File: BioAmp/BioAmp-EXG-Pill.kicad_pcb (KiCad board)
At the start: 4 copper layers, 48.2 x 13.2 mm, 43 parts, among them IC3 MAX1169BEUD+, J1 Conn_01x06_Pin, J2 Conn_01x06_Pin, J4 522710469, U1 TL074HIPWR

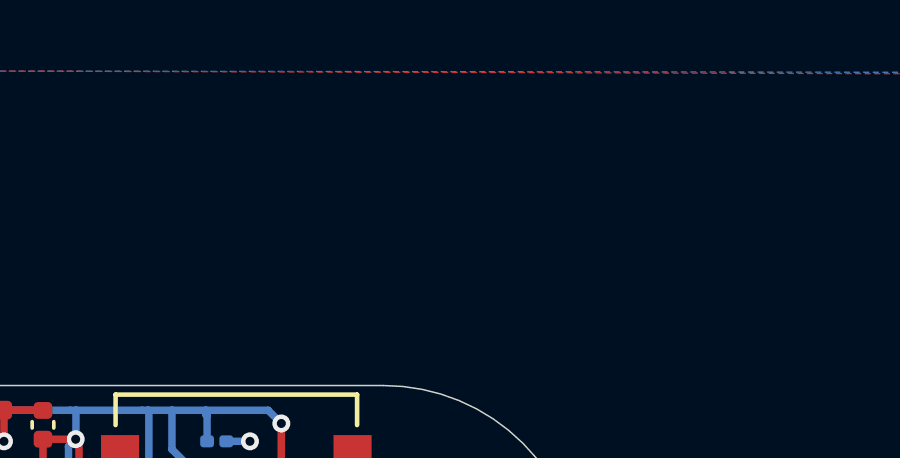
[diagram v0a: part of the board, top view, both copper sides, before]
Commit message: Changed schematics to new ADC ADS
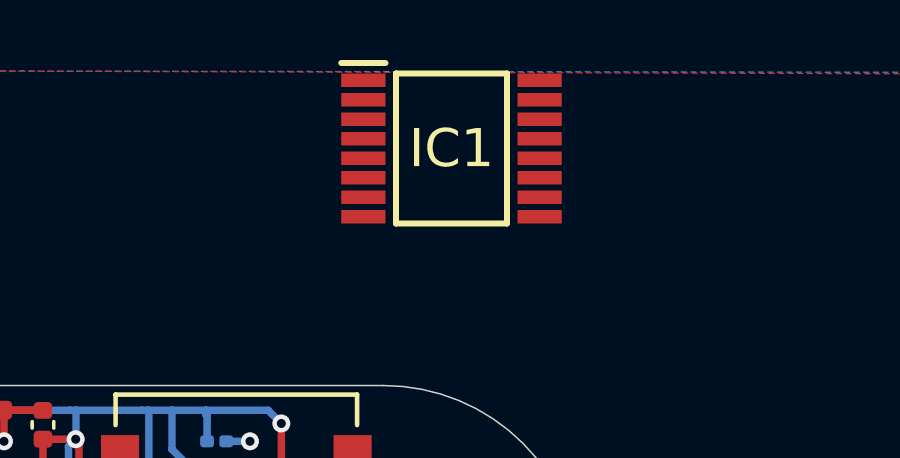
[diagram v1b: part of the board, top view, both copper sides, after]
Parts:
- added IC1: ADS112C04IPW, New_ADS112C04:SOP65P640X120-16N, F.Cu at (147.9, 79.1)

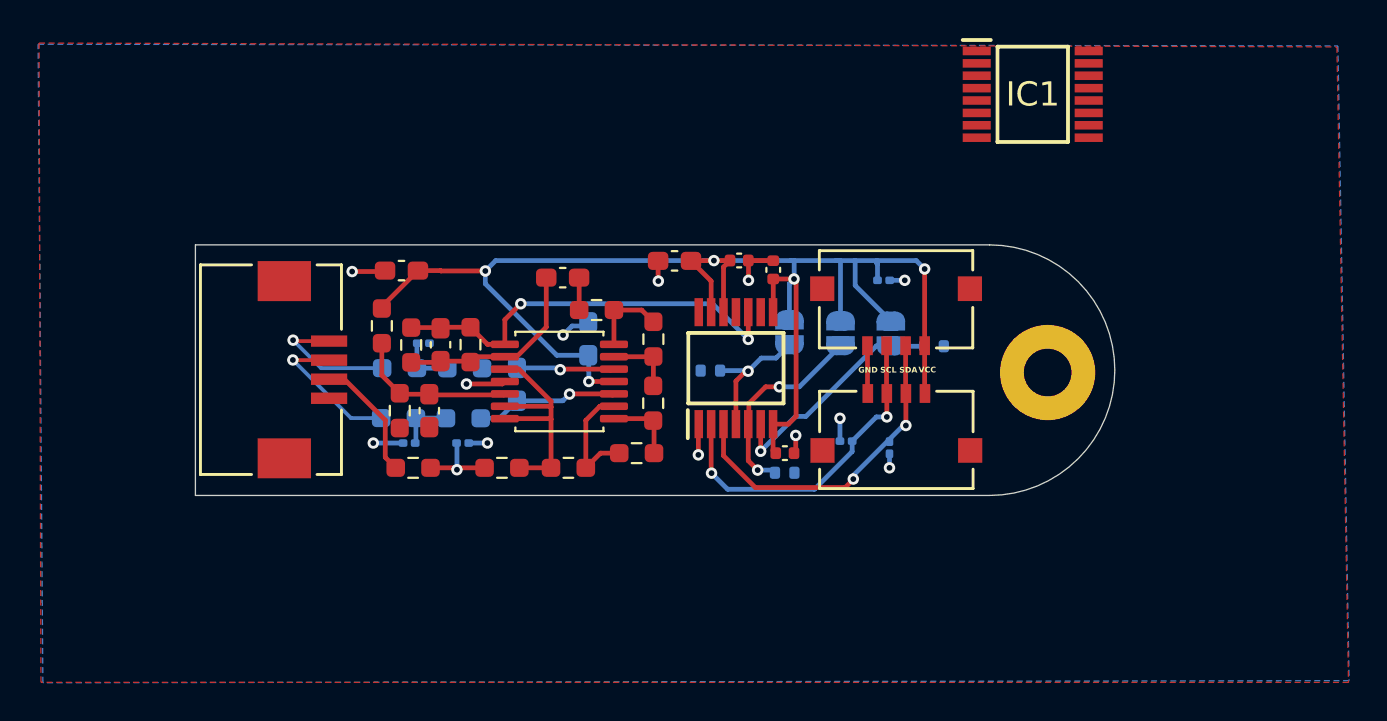
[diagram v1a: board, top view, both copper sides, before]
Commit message: Finished layout with new ADC - ADS
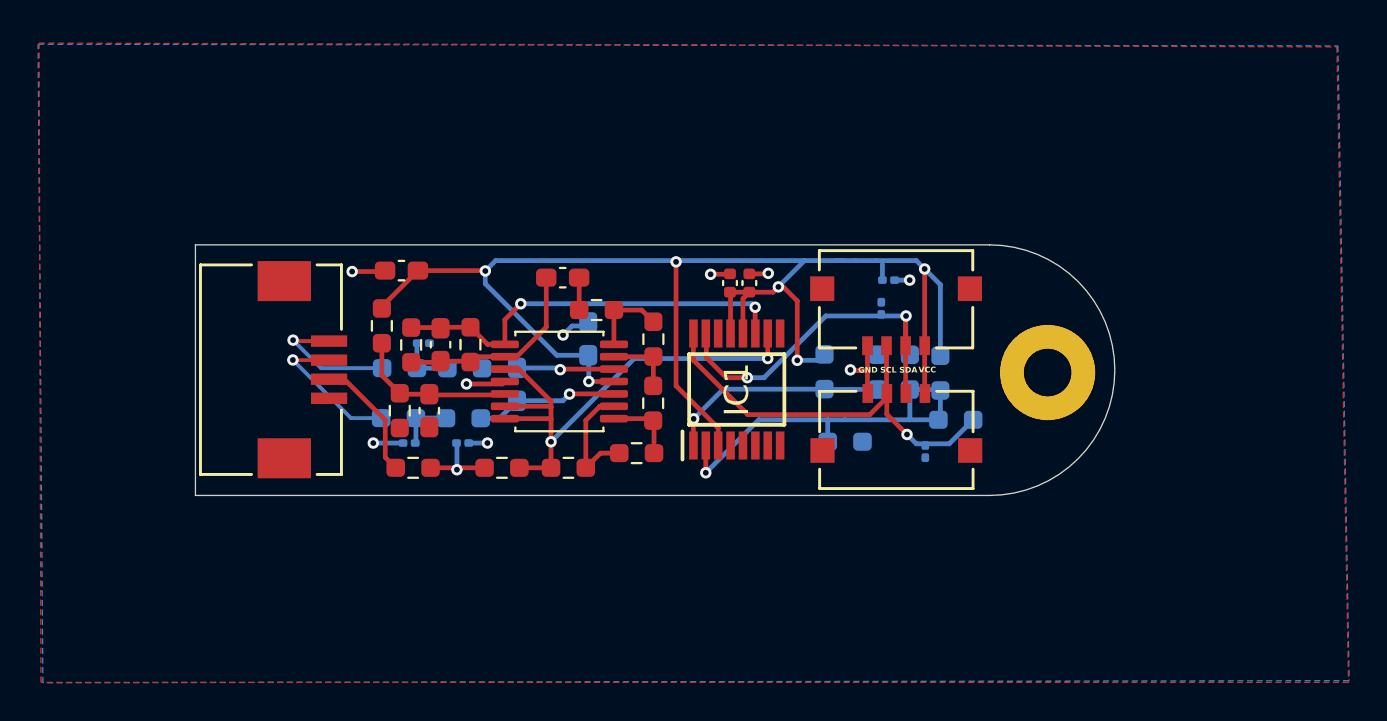
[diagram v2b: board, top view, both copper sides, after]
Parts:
- removed C10: 100n, Capacitor_SMD:C_0402_1005Metric
- removed C12: 10u, Capacitor_SMD:C_0603_1608Metric_Pad1.08x0.95mm_HandSolder
- removed IC3: MAX1169BEUD+, MAX1169:SOP65P640X110-14N
- removed JP4, JP5, JP6: SolderJumper_2_Open, Jumper:SolderJumper-2_P1.3mm_Open_RoundedPad1.0x1.5mm
- added R16: 10k, Resistor_SMD:R_0603_1608Metric_Pad0.98x0.95mm_HandSolder, B.Cu at (137.0, 93.7)
- added R20: 10k, Resistor_SMD:R_0603_1608Metric_Pad0.98x0.95mm_HandSolder, B.Cu at (143.9, 96.2)
- added R21: 10k, Resistor_SMD:R_0603_1608Metric_Pad0.98x0.95mm_HandSolder, B.Cu at (141.5, 93.7)
- R17, R18, R19: footprint Resistor_SMD:R_0402_1005Metric -> Resistor_SMD:R_0603_1608Metric_Pad0.98x0.95mm_HandSolder
- moved IC1 21.9 mm to (132.4, 94.6), turned to 90 degrees
- moved R18 9.70 mm to (143.1, 93.7), turned to -90 degrees
- moved R17 8.77 mm to (139.8, 93.7), turned to 90 degrees
- moved D5 7.33 mm to (140.0, 90.3), turned to 90 degrees
- moved R19 6.85 mm to (138.1, 97.3)
- moved D6 4.20 mm to (142.3, 97.8), turned to -90 degrees
- moved C9 2.37 mm to (132.0, 89.0)
- moved C11 1.30 mm to (133.0, 89.0), turned to -90 degrees
- moved D4 0.26 mm to (140.3, 88.8)
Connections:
- IC1 pad 1: unconnected-(IC1-A0-Pad1) -> /ADD0
- IC1 pad 10: unconnected-(IC1-AIN1-Pad10) -> ampRef
- IC1 pad 11: unconnected-(IC1-AIN0-Pad11) -> bpfOUT
- IC1 pad 12: unconnected-(IC1-AVDD-Pad12) -> VCC
- IC1 pad 13: unconnected-(IC1-DVDD-Pad13) -> VCC
- IC1 pad 15: unconnected-(IC1-SDA-Pad15) -> SDA
- IC1 pad 16: unconnected-(IC1-SCL-Pad16) -> SCL
- IC1 pad 2: unconnected-(IC1-A1-Pad2) -> /ADD1
- IC1 pad 3: unconnected-(IC1-~{RESET}-Pad3) -> VCC
- IC1 pad 4: unconnected-(IC1-DGND-Pad4) -> GND
- IC1 pad 5: unconnected-(IC1-AVSS-Pad5) -> GND
- R17 pad 1: /ADD2 -> /ADD0
- R18 pad 1: /ADD1 -> VCC
- R18 pad 2: GND -> /ADD1
- R19 pad 1: /ADD0 -> /ADD1
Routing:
- net ampRef: track 13.2 -> 27.6 mm, vias 0 -> 2
- net /ADD1: track 10.7 -> 20.9 mm, vias 2 -> 1
- net /ADD2: track 7.53 -> 0.00 mm, vias 1 -> 0
- net GND: track 19.3 -> 14.2 mm, vias 12 -> 9
- net SCL: track 17.8 -> 22.6 mm, vias 2 -> 1
- net SDA: track 17.7 -> 19.8 mm
- net VCC: track 79.1 -> 77.9 mm, vias 5 -> 6
- net /ADD0: track 12.6 -> 11.7 mm

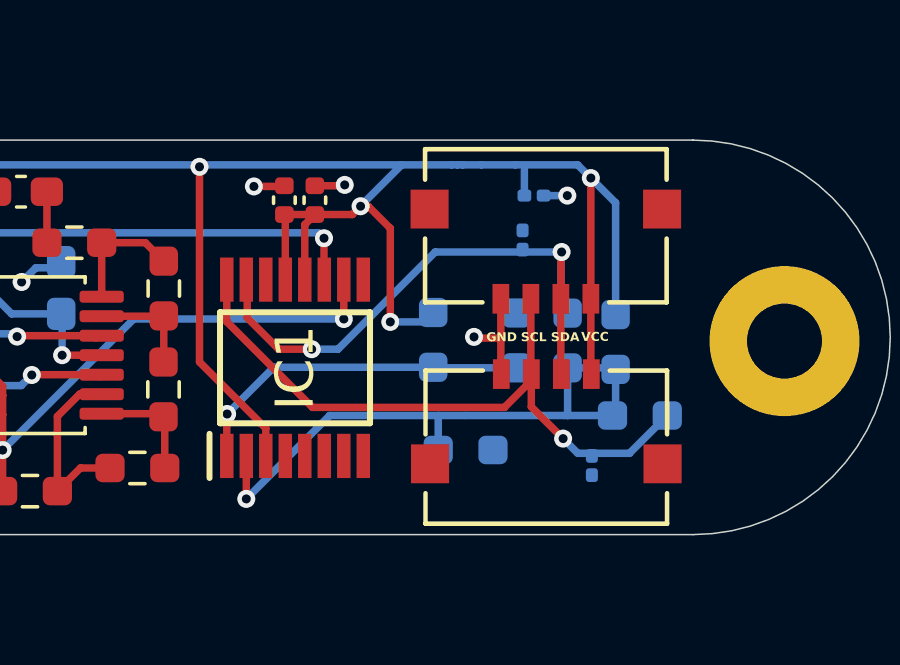
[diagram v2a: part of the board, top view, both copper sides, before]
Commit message: Changed position of TVS on SCL
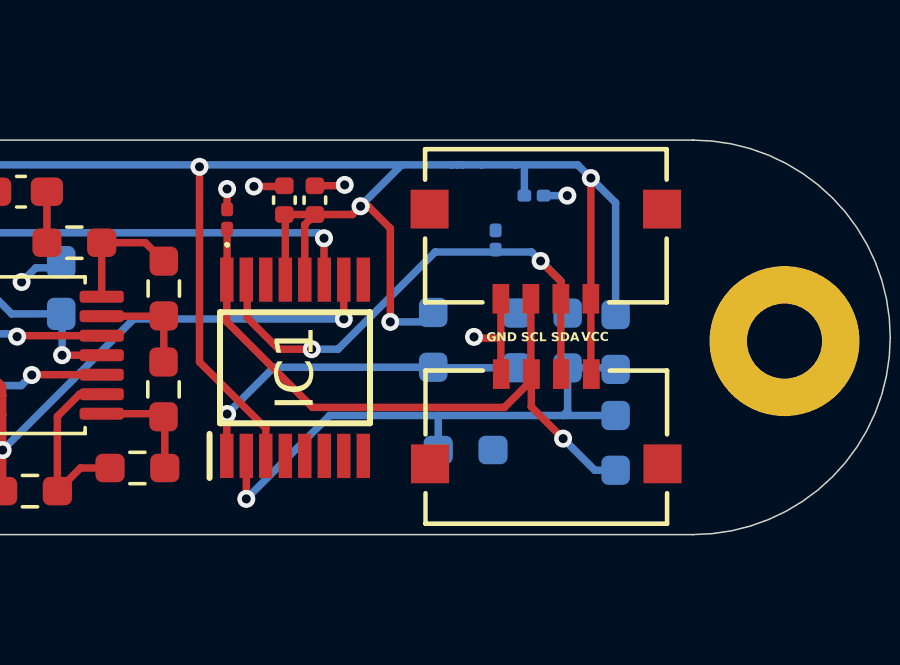
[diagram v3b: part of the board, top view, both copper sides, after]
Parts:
- D6: moved to F.Cu
- moved D6 14.7 mm to (130.1, 89.6), turned to 90 degrees
- moved R20 1.22 mm to (143.1, 97.1), turned to -90 degrees
- moved D5 0.90 mm to (139.1, 90.3)
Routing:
- net /ADD1: track 20.9 -> 19.4 mm
- net GND: track 14.2 -> 14.9 mm, vias 9 -> 10
- net SDA: track 19.8 -> 19.1 mm

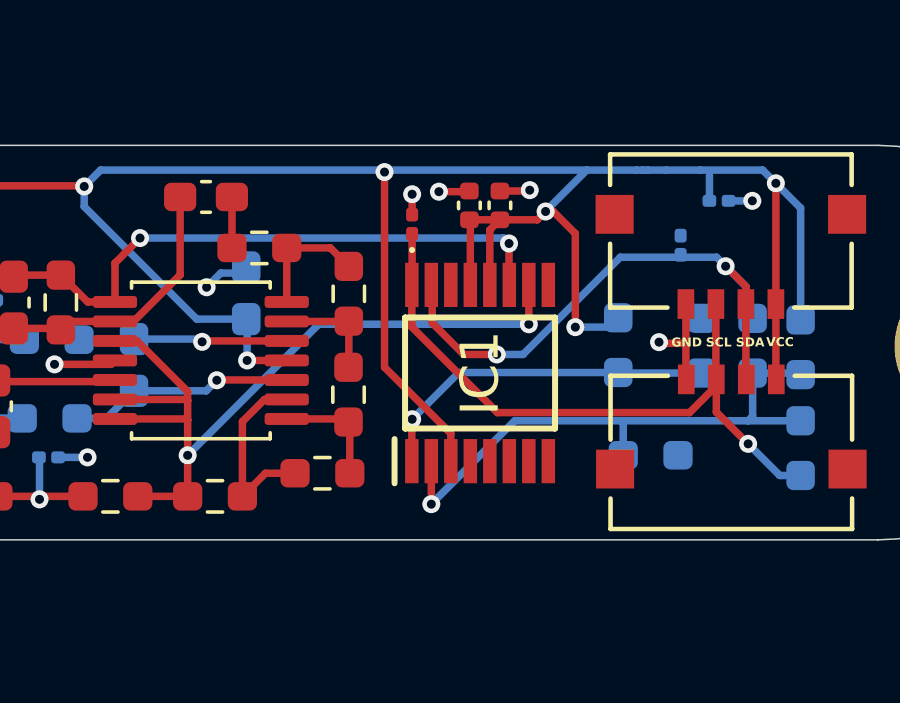
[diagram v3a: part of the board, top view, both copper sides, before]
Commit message: Added via to GND pins on ADC
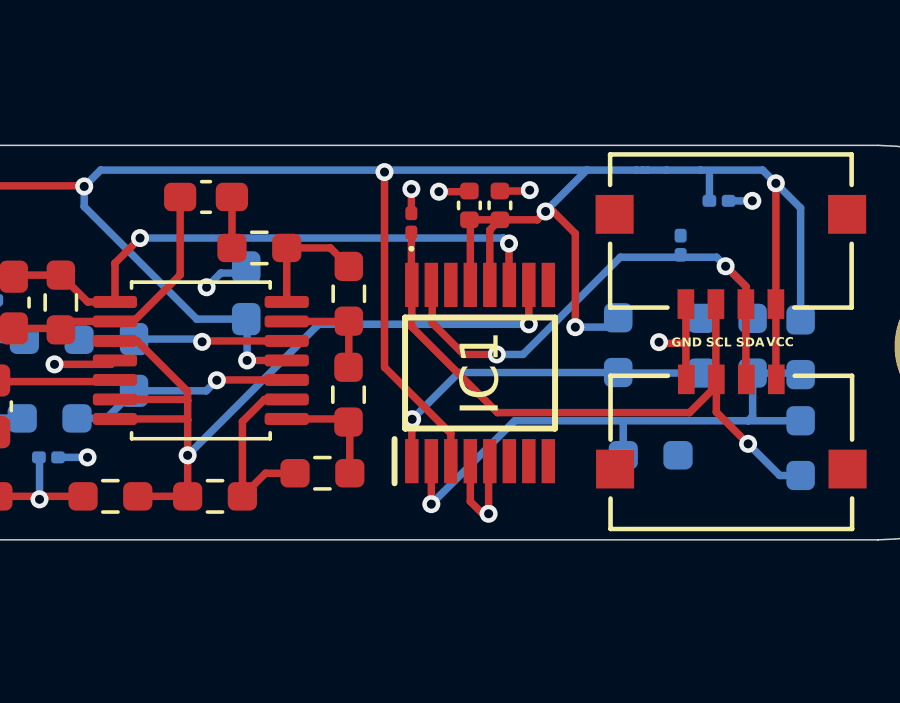
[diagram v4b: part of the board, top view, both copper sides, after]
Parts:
- moved D6 0.05 mm to (130.1, 89.6)
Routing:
- net GND: track 14.9 -> 18.9 mm, vias 10 -> 11
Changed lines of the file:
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@@
 	(footprint "Diode_SMD:D_0201_0603Metric"
 		(layer "F.Cu")
-		(at 130.12 89.63 90)
+		(at 130.095 89.585 90)
 		(descr "Diode SMD 0201 (0603 Metric), square (rectangular) end terminal, IPC-7351 nominal, (Body size source: https://www.vishay.com/docs/20052/crcw0201e3.pdf)")
 		(tags "diode")
@@
 	)
 	(segment
+		(start 132.67 99.28)
+		(end 132.47 99.28)
+		(width 0.25)
+		(layer "F.Cu")
+		(net "GND")
+	)
+	(segment
+		(start 132.0598 98.8698)
+		(end 132.0598 97.5276)
+		(width 0.25)
+		(layer "F.Cu")
+		(net "GND")
+	)
+	(segment
+		(start 130.095 88.455)
+		(end 130.095 89.265)
+		(width 0.25)
+		(layer "F.Cu")
+		(net "GND")
+	)
+	(segment
 		(start 133.0732 88.4936)
 		(end 133.0452 88.5216)
@@
 	)
 	(segment
+		(start 132.67 99.28)
+		(end 132.67 97.5674)
+		(width 0.25)
+		(layer "F.Cu")
+		(net "GND")
+	)
+	(segment
 		(start 134.012 88.5216)
 		(end 134.04 88.4936)
@@
 	)
 	(segment
-		(start 130.12 89.31)
-		(end 130.12 88.63)
+		(start 132.67 97.5674)
+		(end 132.7098 97.5276)
+		(width 0.25)
+		(layer "F.Cu")
+		(net "GND")
+	)
+	(segment
+		(start 132.47 99.28)
+		(end 132.0598 98.8698)
 		(width 0.25)
 		(layer "F.Cu")
@@
 	)
 	(via
-		(at 130.12 88.63)
+		(at 130.095 88.455)
 		(size 0.6)
 		(drill 0.3)
 		(layers "F.Cu" "B.Cu")
+		(free yes)
 		(net "GND")
 	)
@@
 	)
 	(via
+		(at 132.67 99.28)
+		(size 0.6)
+		(drill 0.3)
+		(layers "F.Cu" "B.Cu")
+		(free yes)
+		(net "GND")
+	)
+	(via
 		(at 112.2 88.4)
 		(size 0.6)
@@
 	)
 	(segment
+		(start 130.095 91.6368)
+		(end 130.1098 91.6516)
+		(width 0.25)
+		(layer "F.Cu")
+		(net "SCL")
+	)
+	(segment
 		(start 140.260001 95.890001)
 		(end 140.260001 94.8)
@@
 	)
 	(segment
-		(start 130.1098 93.052973)
-		(end 130.1098 91.6516)
+		(start 130.095 89.905)
+		(end 130.095 91.6368)
 		(width 0.25)
 		(layer "F.Cu")
@@
 	)
 	(segment
-		(start 130.12 89.95)
-		(end 130.12 91.6414)
+		(start 130.1098 93.052973)
+		(end 130.1098 91.6516)
 		(width 0.25)
 		(layer "F.Cu")

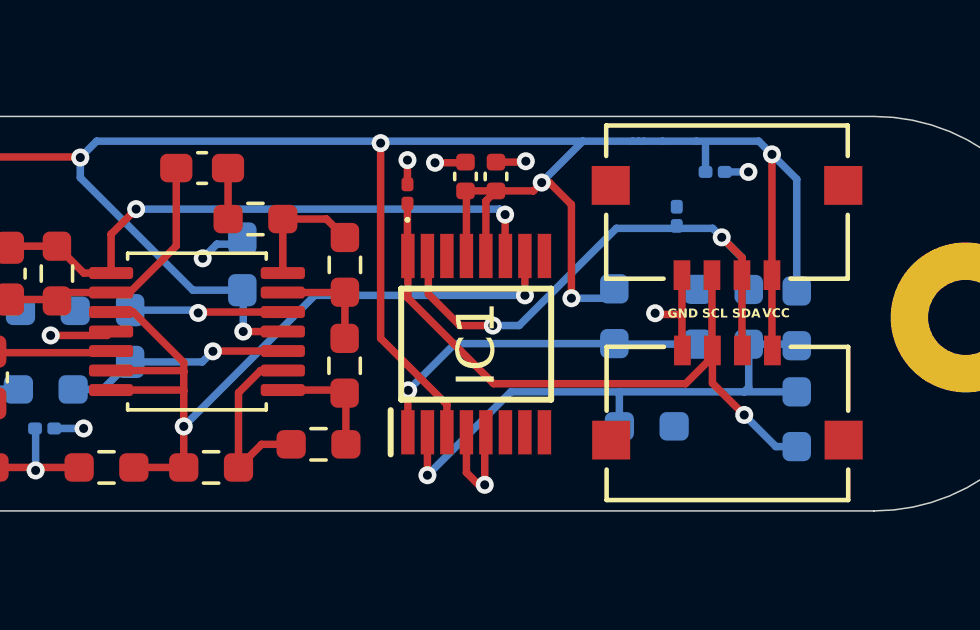
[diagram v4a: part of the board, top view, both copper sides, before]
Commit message: Moved SDA connection
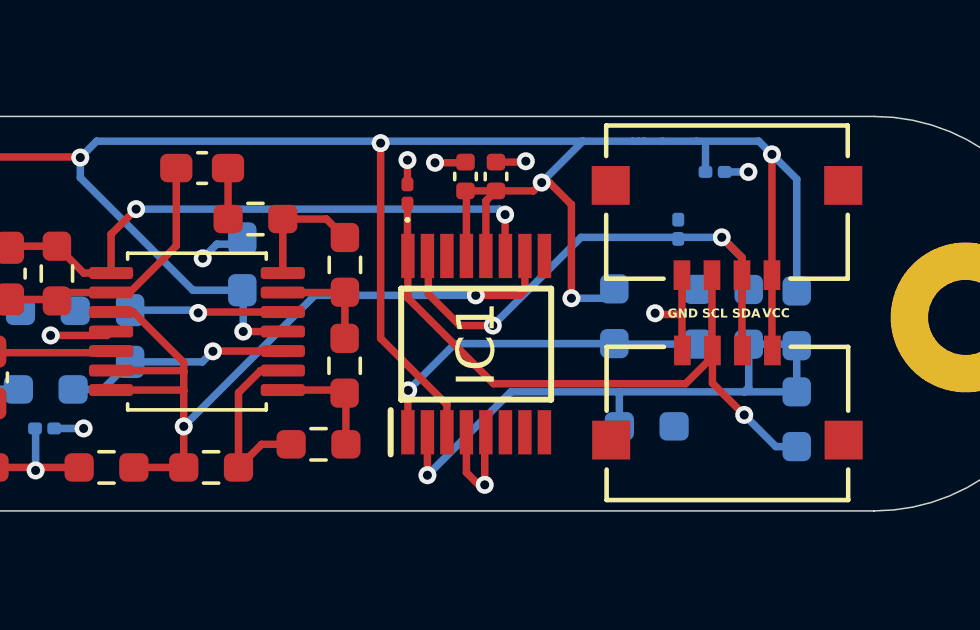
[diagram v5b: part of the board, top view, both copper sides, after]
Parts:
- moved D5 0.44 mm to (139.1, 90.8)
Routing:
- net /ADD1: track 19.4 -> 20.9 mm
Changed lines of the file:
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@@
 	(footprint "Diode_SMD:D_0201_0603Metric"
 		(layer "B.Cu")
-		(at 139.07 90.33 90)
+		(at 139.12 90.7625 90)
 		(descr "Diode SMD 0201 (0603 Metric), square (rectangular) end terminal, IPC-7351 nominal, (Body size source: https://www.vishay.com/docs/20052/crcw0201e3.pdf)")
 		(tags "diode")
@@
 	)
 	(segment
-		(start 133.817573 93.97)
-		(end 132.94 93.97)
+		(start 140.57 91.03)
+		(end 135.88 91.03)
 		(width 0.25)
 		(layer "B.Cu")
@@
 	)
 	(segment
-		(start 137.057573 90.73)
-		(end 133.817573 93.97)
-		(width 0.25)
-		(layer "B.Cu")
-		(net "SDA")
-	)
-	(segment
-		(start 140.57 91.03)
-		(end 140.27 90.73)
-		(width 0.25)
-		(layer "B.Cu")
-		(net "SDA")
-	)
-	(segment
-		(start 140.27 90.73)
-		(end 137.057573 90.73)
+		(start 135.88 91.03)
+		(end 132.94 93.97)
 		(width 0.25)
 		(layer "B.Cu")
@@
 	)
 	(segment
+		(start 133.836 92.964)
+		(end 134.0098 92.7902)
+		(width 0.25)
+		(layer "F.Cu")
+		(net "ampRef")
+	)
+	(segment
 		(start 120.952499 93.52)
 		(end 120.215 93.52)
@@
 	)
 	(segment
-		(start 134.0098 92.9634)
-		(end 134.0104 92.964)
+		(start 134.0098 92.7902)
+		(end 134.0098 91.6516)
 		(width 0.25)
 		(layer "F.Cu")
@@
 	)
 	(segment
-		(start 134.0098 91.6516)
-		(end 134.0098 92.9634)
+		(start 132.37 92.964)
+		(end 133.836 92.964)
 		(width 0.25)
 		(layer "F.Cu")
@@
 	)
 	(via
-		(at 134.0104 92.964)
+		(at 132.37 92.964)
 		(size 0.6)
 		(drill 0.3)
@@
 	(segment
 		(start 127.0063 92.964)
-		(end 134.0104 92.964)
+		(end 122.6375 97.3328)
 		(width 0.25)
 		(layer "B.Cu")
@@
 	)
 	(segment
-		(start 122.6375 97.3328)
+		(start 132.37 92.964)
 		(end 127.0063 92.964)
 		(width 0.25)
@@
 		(width 0.25)
 		(layer "B.Cu")
+		(net "/ADD1")
+	)
+	(segment
+		(start 143.07 96.18)
+		(end 143.07 94.6425)
+		(width 0.25)
+		(layer "B.Cu")
